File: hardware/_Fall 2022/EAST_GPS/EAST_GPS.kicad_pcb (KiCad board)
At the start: 2 copper layers, 30.5 x 25.4 mm, 3 parts, among them J1 Conn_02x08_Odd_Even, U1 GPS-14414, U2 RFM69HCW_Breakout

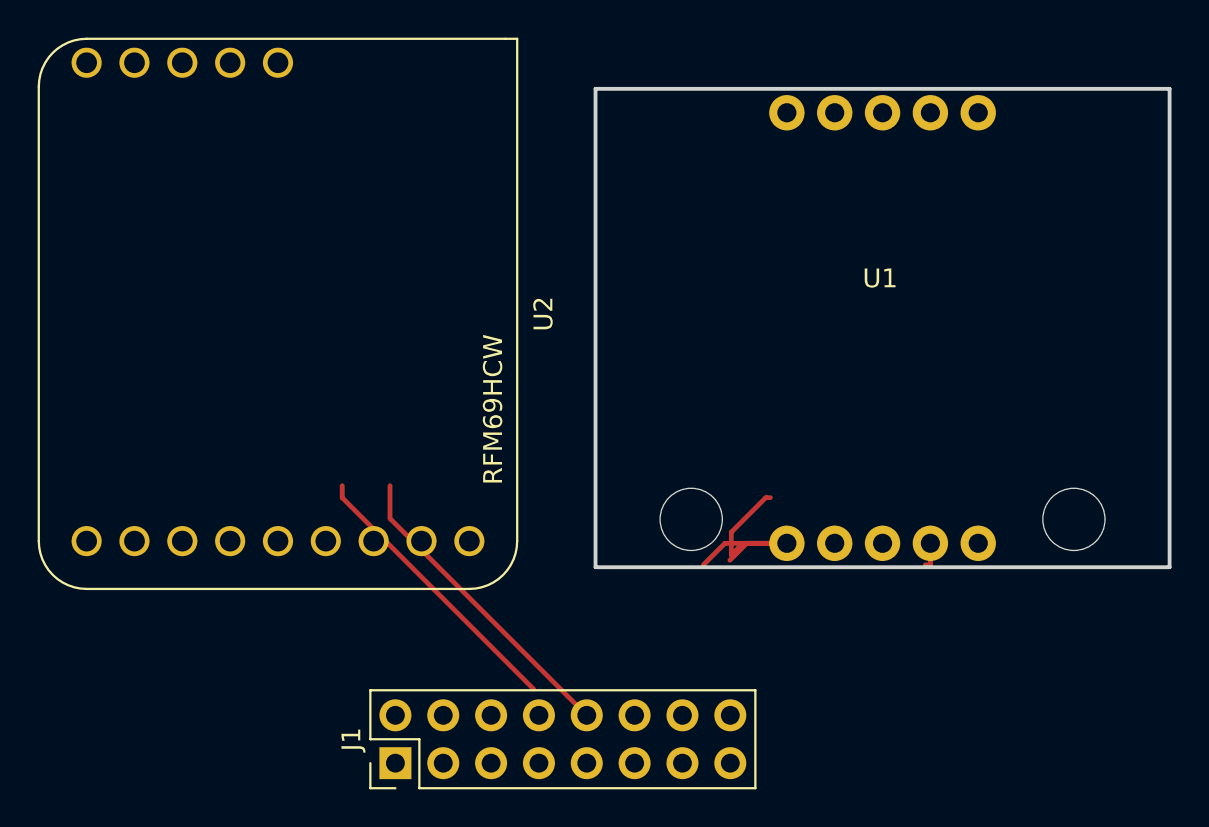
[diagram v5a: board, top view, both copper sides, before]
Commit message: Change gps footprint
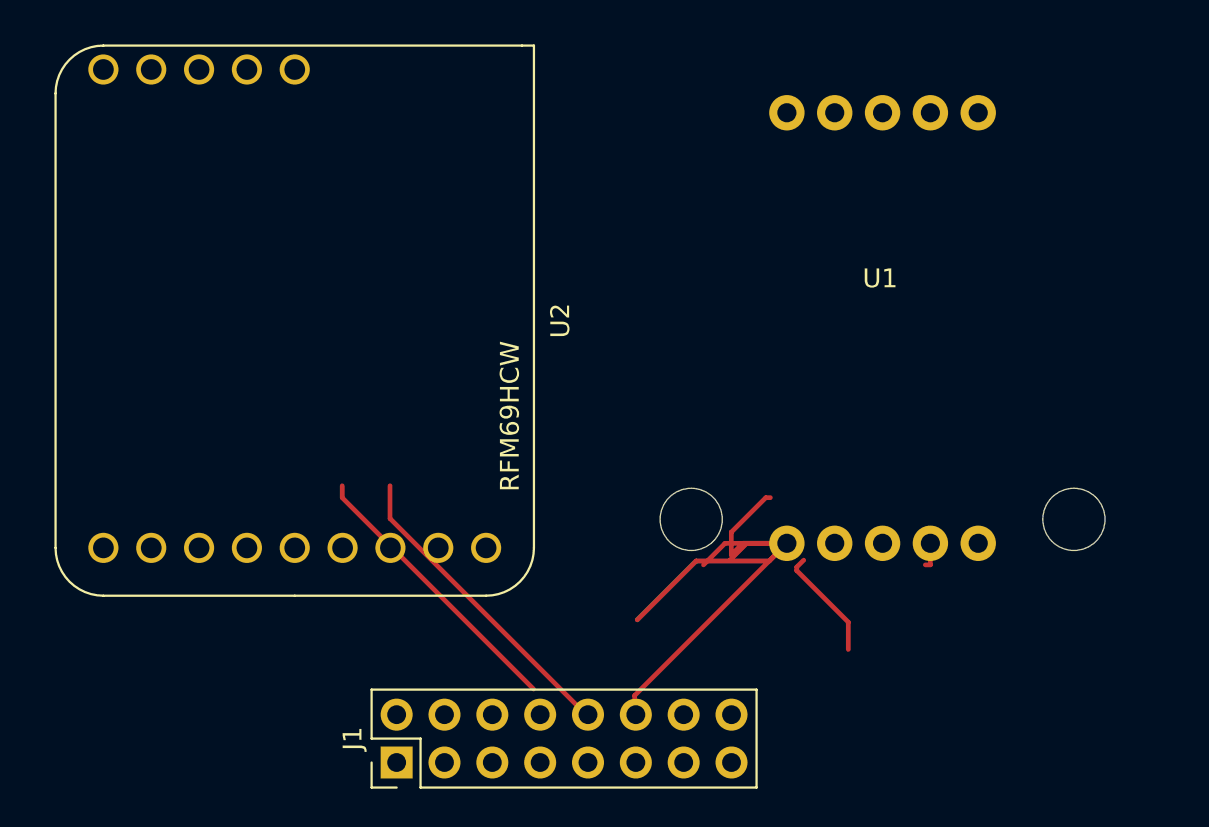
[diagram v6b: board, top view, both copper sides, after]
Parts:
- moved U2 0.96 mm to (127.0, 97.3)
- moved J1 0.07 mm to (132.4, 120.7)
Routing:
- net /SCL 2: track 15.6 -> 47.3 mm
- net /MISO 1: track 31.5 -> 15.0 mm
- net /CS 1: track 0.00 -> 16.5 mm
- net (no net): track 0.00 -> 6.03 mm
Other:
- board outline removed
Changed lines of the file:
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@@
   (net 30 "unconnected-(U1-Pad10)")
   (footprint "Sensors:RFM69HCW_Breakout" (layer "F.Cu")
-    (at 126.13 96.92 -90)
+    (at 127.02 97.28 -90)
     (property "Sheetfile" "EAST_GPS.kicad_sch")
     (property "Sheetname" "")
@@
       (effects (font (size 1 1) (thickness 0.15)))
     )
-    (fp_line (start 15.113 12.573) (end -15.367 12.573) (layer "Edge.Cuts") (width 0.2032))
-    (fp_line (start -15.367 12.573) (end -15.367 -12.827) (layer "Edge.Cuts") (width 0.2032))
-    (fp_line (start -15.367 -12.827) (end 15.113 -12.827) (layer "Edge.Cuts") (width 0.2032))
-    (fp_line (start 15.113 -12.827) (end 15.113 12.573) (layer "Edge.Cuts") (width 0.2032))
+    (fp_line (start -15.367 12.573) (end -15.367 -14) (layer "F.CrtYd") (width 0.2032))
+    (fp_line (start -15.367 -14) (end 15.113 -14) (layer "F.CrtYd") (width 0.2032))
+    (fp_line (start 15.113 12.573) (end -15.367 12.573) (layer "F.CrtYd") (width 0.2032))
+    (fp_line (start 15.113 -14) (end 15.113 12.573) (layer "F.CrtYd") (width 0.2032))
     (fp_circle (center -10.287 -10.287) (end -7.493 -10.287) (layer "F.CrtYd") (width 0.127) (fill none))
     (fp_circle (center 10.033 -10.287) (end 12.827 -10.287) (layer "F.CrtYd") (width 0.127) (fill none))
-    (fp_poly (pts
-        (xy 14.986 12.954)
-        (xy 15.494 12.954)
-        (xy 15.494 12.446)
-        (xy 14.986 12.446)
-      ) (layer "F.Fab") (width 0) (fill solid))
     (pad "" np_thru_hole circle (at -10.287 -10.287 180) (size 3.302 3.302) (drill 3.302) (layers *.Cu *.Mask))
     (pad "" np_thru_hole circle (at 10.033 -10.287 180) (size 3.302 3.302) (drill 3.302) (layers *.Cu *.Mask))
@@
   )
   (footprint "Connector_PinHeader_2.54mm:PinHeader_2x08_P2.54mm_Vertical" (layer "F.Cu")
-    (at 132.365 120.775 90)
+    (at 132.43 120.74 90)
     (descr "Through hole straight pin header, 2x08, 2.54mm pitch, double rows")
     (tags "Through hole pin header THT 2x08 2.54mm double row")
@@
     )
     (fp_line (start -1.33 1.27) (end 1.27 1.27) (layer "F.SilkS") (width 0.12))
+    (fp_line (start -1.33 0) (end -1.33 -1.33) (layer "F.SilkS") (width 0.12))
+    (fp_line (start -1.33 -1.33) (end 0 -1.33) (layer "F.SilkS") (width 0.12))
+    (fp_line (start -1.33 19.11) (end 3.87 19.11) (layer "F.SilkS") (width 0.12))
+    (fp_line (start 3.87 -1.33) (end 3.87 19.11) (layer "F.SilkS") (width 0.12))
+    (fp_line (start 1.27 1.27) (end 1.27 -1.33) (layer "F.SilkS") (width 0.12))
+    (fp_line (start -1.33 1.27) (end -1.33 19.11) (layer "F.SilkS") (width 0.12))
     (fp_line (start 1.27 -1.33) (end 3.87 -1.33) (layer "F.SilkS") (width 0.12))
-    (fp_line (start -1.33 1.27) (end -1.33 19.11) (layer "F.SilkS") (width 0.12))
-    (fp_line (start -1.33 19.11) (end 3.87 19.11) (layer "F.SilkS") (width 0.12))
-    (fp_line (start -1.33 0) (end -1.33 -1.33) (layer "F.SilkS") (width 0.12))
-    (fp_line (start 1.27 1.27) (end 1.27 -1.33) (layer "F.SilkS") (width 0.12))
-    (fp_line (start 3.87 -1.33) (end 3.87 19.11) (layer "F.SilkS") (width 0.12))
-    (fp_line (start -1.33 -1.33) (end 0 -1.33) (layer "F.SilkS") (width 0.12))
+    (fp_line (start 4.35 19.55) (end 4.35 -1.8) (layer "F.CrtYd") (width 0.05))
+    (fp_line (start -1.8 -1.8) (end -1.8 19.55) (layer "F.CrtYd") (width 0.05))
+    (fp_line (start 4.35 -1.8) (end -1.8 -1.8) (layer "F.CrtYd") (width 0.05))
     (fp_line (start -1.8 19.55) (end 4.35 19.55) (layer "F.CrtYd") (width 0.05))
-    (fp_line (start 4.35 19.55) (end 4.35 -1.8) (layer "F.CrtYd") (width 0.05))
-    (fp_line (start 4.35 -1.8) (end -1.8 -1.8) (layer "F.CrtYd") (width 0.05))
-    (fp_line (start -1.8 -1.8) (end -1.8 19.55) (layer "F.CrtYd") (width 0.05))
-    (fp_line (start -1.27 0) (end 0 -1.27) (layer "F.Fab") (width 0.1))
+    (fp_line (start 3.81 -1.27) (end 3.81 19.05) (layer "F.Fab") (width 0.1))
+    (fp_line (start -1.27 19.05) (end -1.27 0) (layer "F.Fab") (width 0.1))
     (fp_line (start 0 -1.27) (end 3.81 -1.27) (layer "F.Fab") (width 0.1))
     (fp_line (start 3.81 19.05) (end -1.27 19.05) (layer "F.Fab") (width 0.1))
-    (fp_line (start -1.27 19.05) (end -1.27 0) (layer "F.Fab") (width 0.1))
-    (fp_line (start 3.81 -1.27) (end 3.81 19.05) (layer "F.Fab") (width 0.1))
+    (fp_line (start -1.27 0) (end 0 -1.27) (layer "F.Fab") (width 0.1))
     (pad "1" thru_hole rect (at 0 0 90) (size 1.7 1.7) (drill 1) (layers *.Cu *.Mask)
       (net 10 "/RX 2") (pinfunction "Pin_1") (pintype "passive"))
@@
   (gr_line (start 128.8288 116.8654) (end 154.2288 116.8654) (layer "Dwgs.User") (width 0.2))
   (gr_line (start 116.328019 128.2954) (end 166.729581 128.2954) (layer "Dwgs.User") (width 0.2))
+  (segment (start 153.673598 110.553598) (end 153.673598 110.36655) (width 0.25) (layer "F.Cu") (net 0))
+  (segment (start 153.673598 110.36655) (end 154.044049 109.996099) (width 0.25) (layer "F.Cu") (net 0))
+  (segment (start 156.41 114.74) (end 156.41 113.29) (width 0.25) (layer "F.Cu") (net 0))
+  (segment (start 156.41 113.29) (end 153.673598 110.553598) (width 0.25) (layer "F.Cu") (net 0))
   (segment (start 160.7697 110.24675) (end 160.5 110.24675) (width 0.25) (layer "F.Cu") (net 1))
   (segment (start 160.7697 109.10175) (end 160.7697 110.24675) (width 0.25) (layer "F.Cu") (net 1))
-  (segment (start 132.08 107.79) (end 142.525 118.235) (width 0.25) (layer "F.Cu") (net 4))
   (segment (start 139.7 116.84) (end 129.54 106.68) (width 0.25) (layer "F.Cu") (net 4))
-  (segment (start 132.08 106.045) (end 132.08 107.79) (width 0.25) (layer "F.Cu") (net 4))
   (segment (start 129.54 106.68) (end 129.54 106.045) (width 0.25) (layer "F.Cu") (net 4))
+  (segment (start 132.08 107.79) (end 142.525 118.235) (width 0.25) (layer "F.Cu") (net 6))
+  (segment (start 132.08 106.045) (end 132.08 107.79) (width 0.25) (layer "F.Cu") (net 6))
   (segment (start 150.81825 109.10175) (end 150.2 109.72) (width 0.25) (layer "F.Cu") (net 14))
   (segment (start 149.865 109.10175) (end 148.72 110.24675) (width 0.25) (layer "F.Cu") (net 14))
@@
   (segment (start 150.2 109.72) (end 150.2 108.51) (width 0.25) (layer "F.Cu") (net 14))
   (segment (start 152.032 106.678) (end 152.273 106.678) (width 0.25) (layer "F.Cu") (net 14))
+  (segment (start 148.328451 110.041549) (end 145.205 113.165) (width 0.25) (layer "F.Cu") (net 14))
+  (segment (start 153.1497 109.10175) (end 152.209901 110.041549) (width 0.25) (layer "F.Cu") (net 14))
   (segment (start 151.01825 109.10175) (end 153.1497 109.10175) (width 0.25) (layer "F.Cu") (net 14))
+  (segment (start 152.209901 110.041549) (end 148.328451 110.041549) (width 0.25) (layer "F.Cu") (net 14))
   (segment (start 153.1497 109.10175) (end 150.81825 109.10175) (width 0.25) (layer "F.Cu") (net 14))
   (segment (start 153.1497 109.10175) (end 149.865 109.10175) (width 0.25) (layer "F.Cu") (net 14))
   (segment (start 151.01825 109.10175) (end 150.12 110) (width 0.25) (layer "F.Cu") (net 14))
+  (segment (start 145.065 117.18645) (end 145.065 118.235) (width 0.25) (layer "F.Cu") (net 14))
+  (segment (start 153.1497 109.10175) (end 145.065 117.18645) (width 0.25) (layer "F.Cu") (net 14))
+  (segment (start 148.328451 110.041549) (end 145.205 113.165) (width 0.25) (layer "B.Cu") (net 14))
+  (segment (start 153.1497 109.10175) (end 152.209901 110.041549) (width 0.25) (layer "B.Cu") (net 14))
+  (segment (start 152.209901 110.041549) (end 148.328451 110.041549) (width 0.25) (layer "B.Cu") (net 14))
   (group "" (id 16c30f42-175b-400f-b540-6040af78e635)
     (members

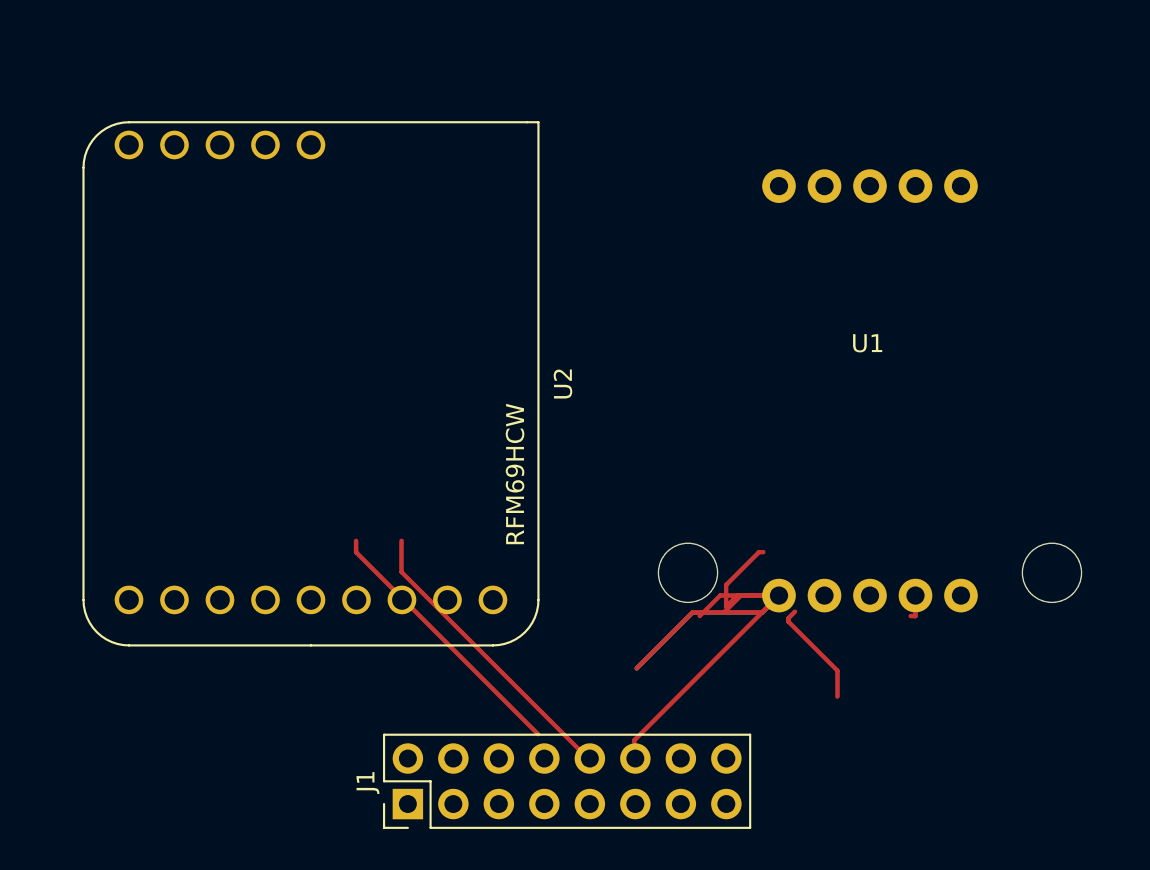
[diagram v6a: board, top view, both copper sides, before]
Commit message: Update EAST connectors
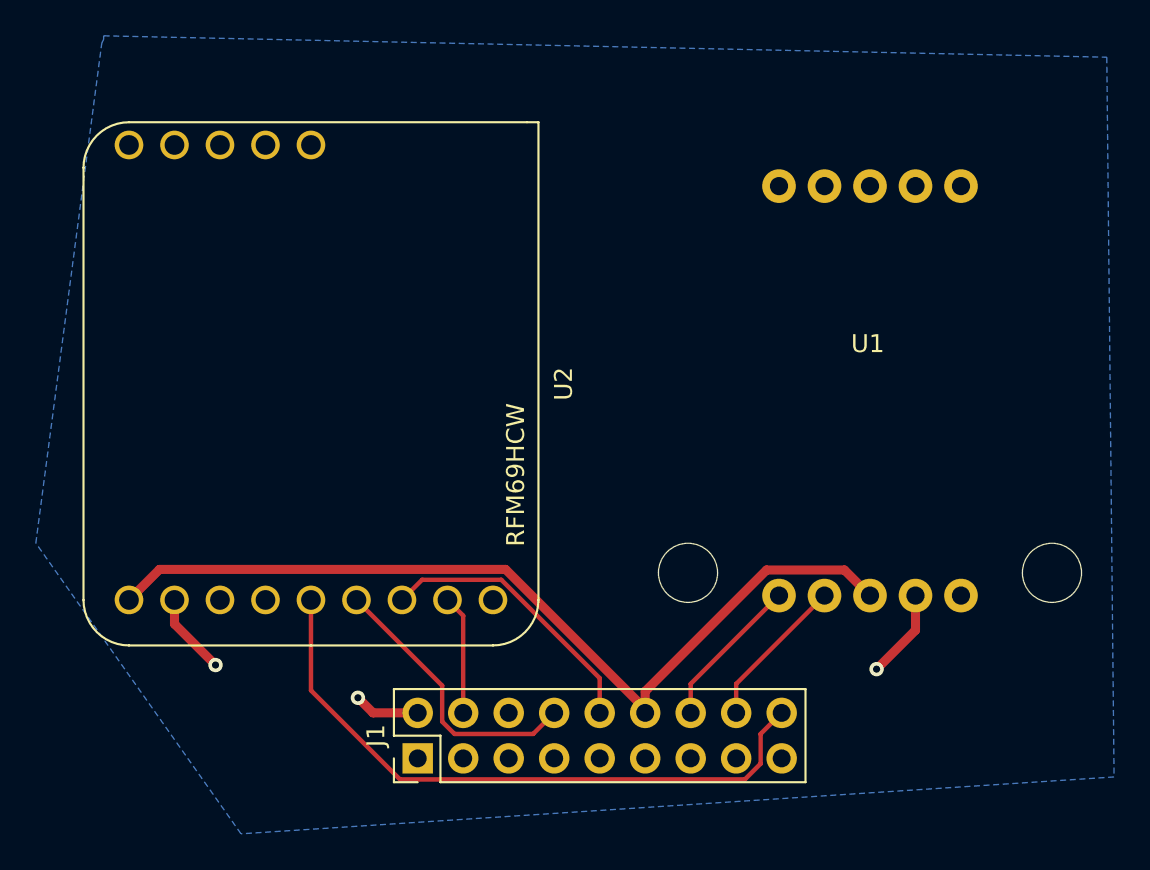
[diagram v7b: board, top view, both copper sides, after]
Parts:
- J1: value Conn_02x08_Odd_Even -> Conn_02x09_Odd_Even; footprint Connector_PinHeader_2.54mm:PinHeader_2x08_P2.54mm_Vertical -> Connector_PinHeader_2.54mm:PinHeader_2x09_P2.54mm_Vertical
- moved J1 2.61 mm to (133.0, 118.2)
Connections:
- J1 pad 1: /RX 2 -> /V_BATT
- J1 pad 12: /SCL 2 -> /3.3V
- J1 pad 14: /SDA 2 -> /SCL 2
- J1 pad 16: /SCK 1 -> /SDA 2
- J1 pad 3: /TX 2 -> /RX 2
- J1 pad 5: /SCL 1 -> /TX 2
- J1 pad 7: /SDA 1 -> /SCL 1
- J1 pad 9: /3.3V -> /SDA 1
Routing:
- net /3.3V: track 0.00 -> 50.1 mm
- net /SCL 2: track 47.3 -> 8.59 mm
- net /SCK 1: track 0.00 -> 35.9 mm
- net /MOSI 1: track 0.00 -> 15.8 mm
- net /GND: track 1.41 -> 13.3 mm, vias 0 -> 3
- net /CS 1: track 16.5 -> 6.67 mm
- net /SDA 2: track 0.00 -> 8.59 mm
- net (no net): track 6.03 -> 0.00 mm
- net /MISO 1: track 15.0 -> 15.7 mm
- added copper zone on B.Cu, net /GND

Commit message: logos
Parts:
- added ?: LOGO, LOGO, F.Cu at (130.4, 127.4)
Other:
- board outline added: 76.2 x 66.7 mm
